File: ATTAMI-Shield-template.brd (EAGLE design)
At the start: 22.8 x 22.9 mm, 3 parts, among them J1 CON_HEADER_1X02-PTH, J3 CON_HEADER_1X02-PTH, J4 CON_HEADER_1X06-PTH

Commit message: template for v17
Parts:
- removed J4: CON_HEADER_1X06-PTH, dp_devices:M1X6
- added J2: (no value), microbuilder:1X02_ROUND
- J1: value CON_HEADER_1X02-PTH -> (none); device dp_devices:M1X2 -> microbuilder:1X02_ROUND
- J3: value CON_HEADER_1X02-PTH -> (none); device dp_devices:M1X2 -> microbuilder:1X07_ROUND
- moved J3 21.3 mm to (1.27, 8.89)
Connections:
- new net GND: J1.2, J2.2, J3.1
- new net PB0: J3.2
- new net PB1: J3.3
- new net PB2: J3.4
- new net PB3: J3.5
- new net PB4: J3.6
- new net PB5: J3.7
- new net VBAT: J1.1
- new net VCC: J2.1
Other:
- board text added: "J2"

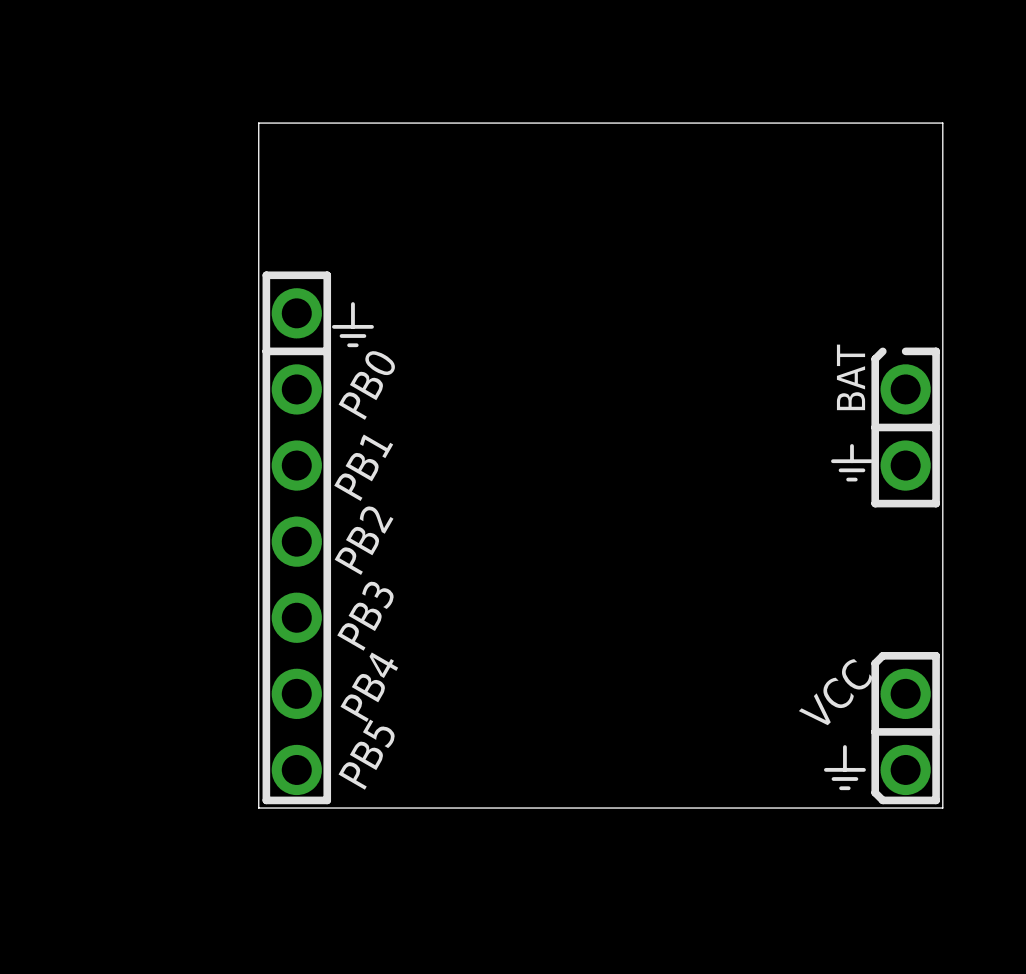
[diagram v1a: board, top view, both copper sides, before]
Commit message: same shield, with added mounting holes and better naming based on ver 0.00
based on attami ver 0.00

https://github.com/telavivmakers/at-tami/commit/00271a633f93de088d04ac549667f0e04d0c47cf#diff-2c24cc5344d8d061ae0f0b1c47d7ba8a
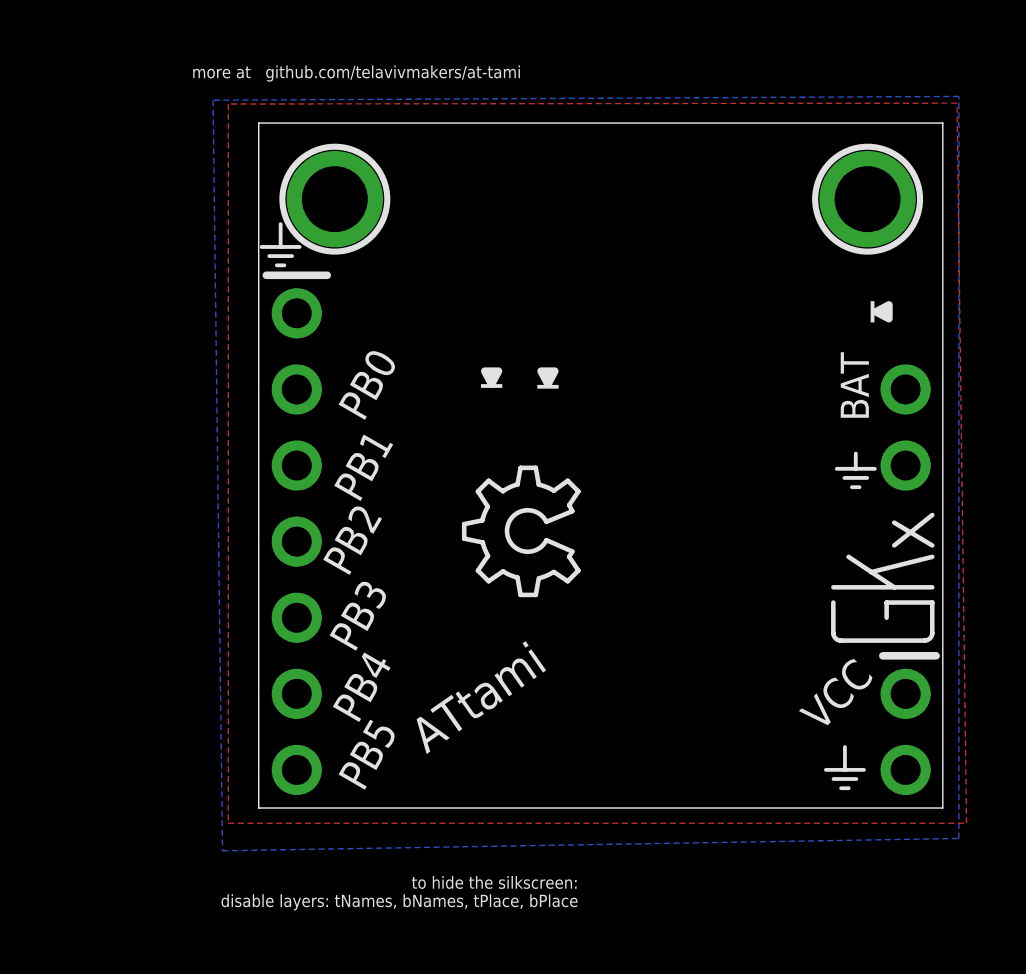
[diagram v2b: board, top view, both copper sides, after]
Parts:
- added U$1, U$2: MOUNTINGHOLE2.0, microbuilder:MOUNTINGHOLE_2.0_PLATED
- added U$3: (no value), ohw-logo:OSHW_6X150_NOTEXT
- J1: device microbuilder:1X02_ROUND -> microbuilder:1X07_ROUND
- J3: device microbuilder:1X07_ROUND -> microbuilder:1X02_ROUND
- moved J3 21.3 mm to (21.6, 2.54)
- moved J1 20.7 mm to (1.27, 8.89)
- moved J2 10.2 mm to (21.6, 12.7)
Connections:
- removed net PB0: J3.2
- removed net PB1: J3.3
- removed net PB2: J3.4
- removed net PB3: J3.5
- removed net PB4: J3.6
- removed net PB5: J3.7
- removed net VBAT: J1.1
- new net N$1: J1.2
- new net N$3: J2.1
- new net N$4: J1.3
- new net N$5: J1.4
- new net N$6: J1.5
- new net N$7: J1.6
- new net N$8: J1.7
- net GND: now also J1.1, J3.2; no longer J1.2, J3.1
- net VCC: now also J3.1; no longer J2.1
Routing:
- added copper zone on layer 1, net GND
- added copper zone on layer 16, net GND
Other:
- board text added: "+"
- board text added: "ATTami V0.00"
- board text added: "ATtami"
- board text added: "more at github.com/telavivmakers/at-tami"
- board text added: "to hide the silkscreen: disable layers: tNames, bNames, tPlace, bPlace"

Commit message: servo shield - new
also added names and labels on wires
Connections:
- net N$1 renamed PB0
- net N$4 renamed PB1
- net N$5 renamed PB2
- net N$6 renamed PB3
- net N$7 renamed PB4
- net N$8 renamed PB5
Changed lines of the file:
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@@
 <contactref element="J2" pad="1"/>
 </signal>
-<signal name="N$1">
+<signal name="PB0">
 <contactref element="J1" pad="2"/>
 </signal>
-<signal name="N$4">
+<signal name="PB1">
 <contactref element="J1" pad="3"/>
 </signal>
-<signal name="N$5">
+<signal name="PB2">
 <contactref element="J1" pad="4"/>
 </signal>
-<signal name="N$6">
+<signal name="PB3">
 <contactref element="J1" pad="5"/>
 </signal>
-<signal name="N$7">
+<signal name="PB4">
 <contactref element="J1" pad="6"/>
 </signal>
-<signal name="N$8">
+<signal name="PB5">
 <contactref element="J1" pad="7"/>
 </signal>
